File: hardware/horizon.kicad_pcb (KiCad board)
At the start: 2 copper layers, 95 x 56.2 mm, 31 parts, among them J1 Conn_01x02_Pin, J2 Conn_01x06_Pin, J3 USB_C_Receptacle_USB2.0_14P, J4 Conn_01x14_Pin, J6 Conn_01x02_Pin, SW1 SW_Push, U1 ESP32-S3, U2 NCP1529A, U3 W25Q128JVS, U4 BQ24074RGT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

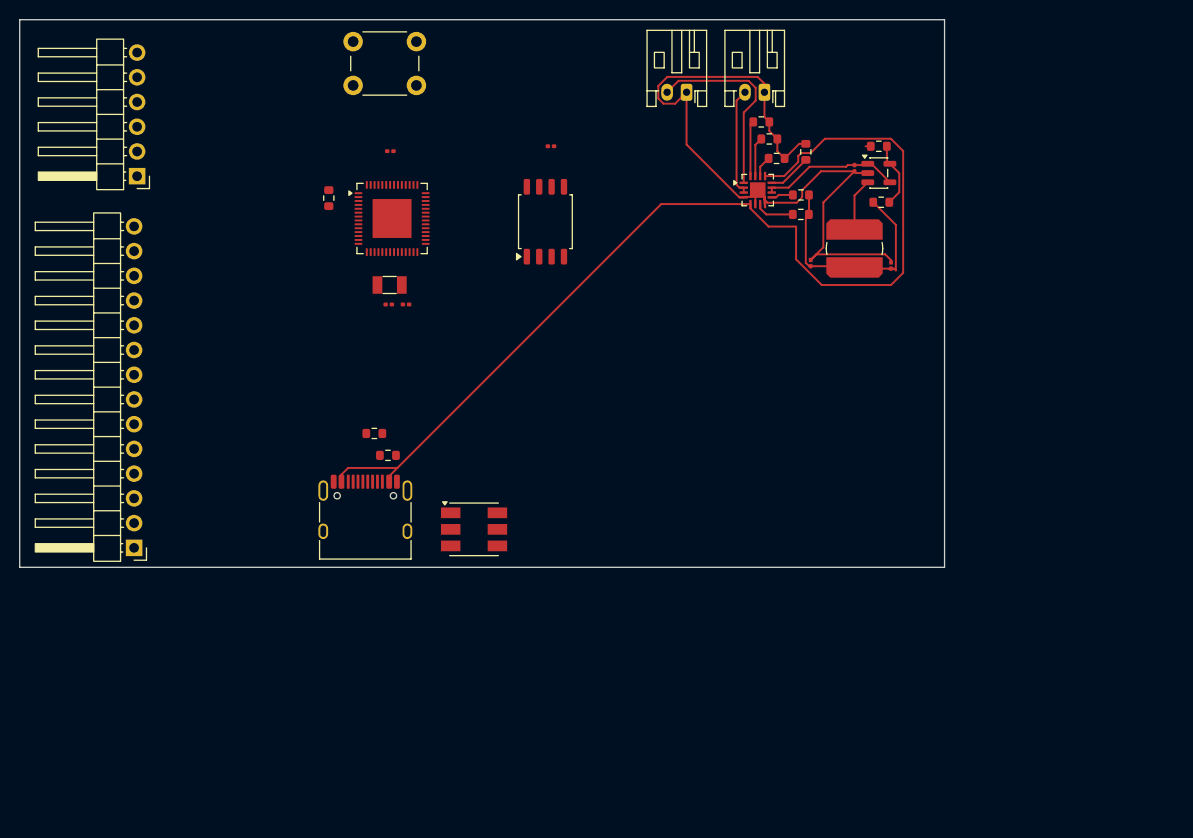
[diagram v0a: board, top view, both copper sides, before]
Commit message: added antenna
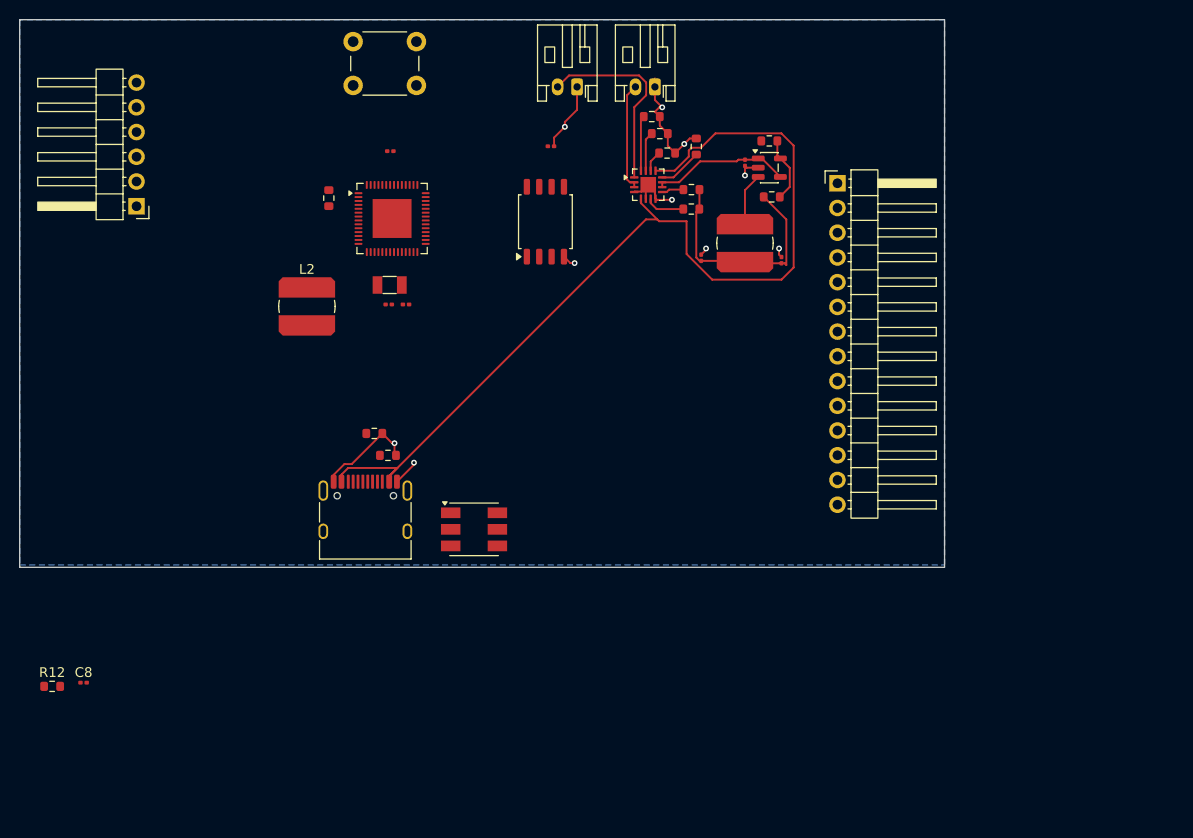
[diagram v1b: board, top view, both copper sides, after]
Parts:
- added C8: DNP, Capacitor_SMD:C_0201_0603Metric, F.Cu at (96.6, 93.1)
- added L2: DNP, Inductor_SMD:L_Bourns_SDR0604, F.Cu at (119.5, 54.5)
- added R12: 0R, Resistor_SMD:R_0603_1608Metric, F.Cu at (93.3, 93.5)
- moved J4 81.4 mm to (174.0, 41.8), turned to 0 degrees
- moved C3 11.3 mm to (164.5, 39.7)
- moved C4 11.3 mm to (168.2, 49.7)
- moved C5 11.3 mm to (160.0, 49.5)
- moved J1 11.3 mm to (147.2, 31.9)
- moved J6 11.3 mm to (155.2, 31.9)
- moved L1 11.3 mm to (164.5, 48.0)
- moved R1 11.3 mm to (167.2, 43.2)
- moved R10 11.3 mm to (159.0, 44.5)
- moved R11 11.3 mm to (156.5, 38.7)
- moved R2 11.3 mm to (167.0, 37.5)
- moved R6 11.3 mm to (159.5, 38.0)
- moved R7 11.3 mm to (154.9, 35.0)
- moved R8 11.3 mm to (155.8, 36.7)
- moved R9 11.3 mm to (159.0, 42.5)
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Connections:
- U1 pad 1: unconnected-(U1-LNA_IN-Pad1) -> Net-(U1-LNA_IN)
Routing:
- net GND: track 81.4 -> 46.7 mm, vias 0 -> 10
- net Net-(U4-EN2): track 107.1 -> 98.0 mm
- added copper zone on B.Cu, net GND

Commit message: Finished prototype pcb
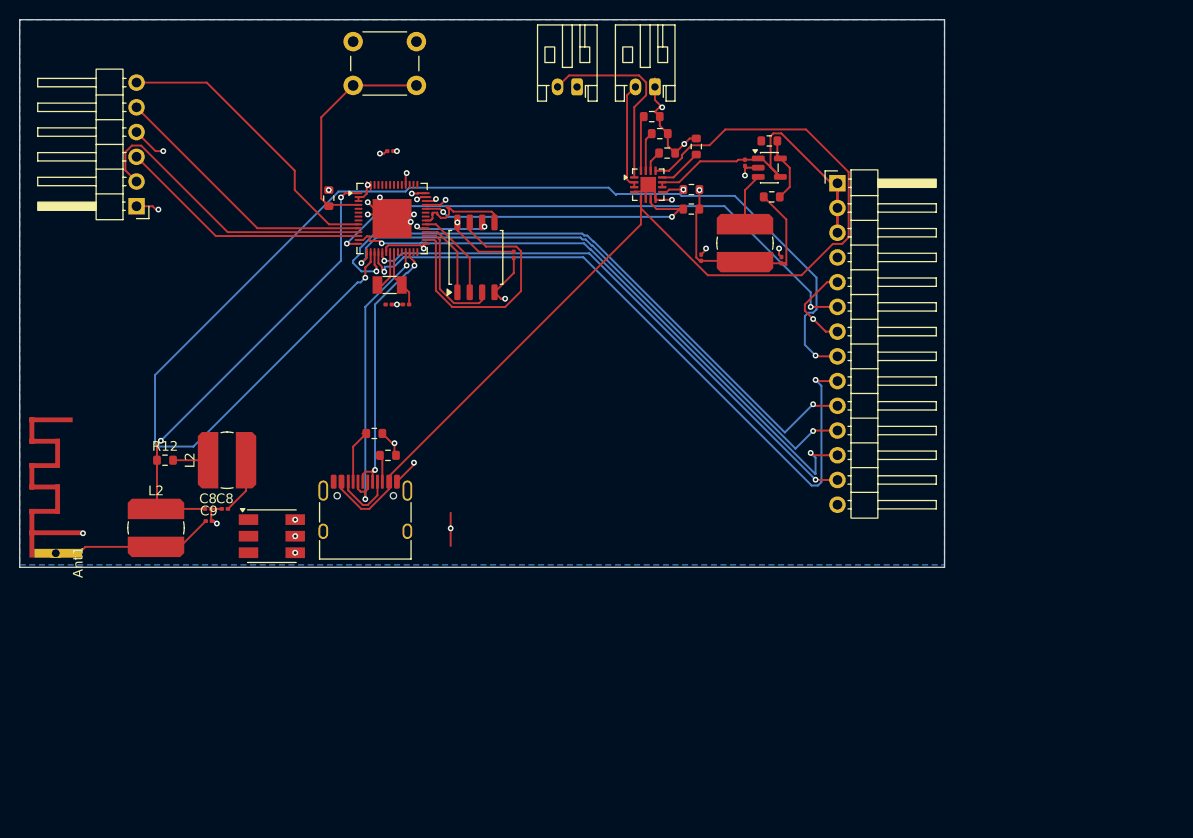
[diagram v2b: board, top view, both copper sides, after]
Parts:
- added Ant1: PCB_Antenna:PCB_Antenna, PCB_Antenna:PCB_Antenna, F.Cu at (96.5, 80.8)
- added C8: 3P3, Capacitor_SMD:C_0201_0603Metric, F.Cu at (109.3, 75.2)
- added C9: 3P3, Capacitor_SMD:C_0201_0603Metric, F.Cu at (109.4, 76.5)
- added L2: 2n2, Inductor_SMD:L_Bourns_SDR0604, F.Cu at (104.0, 77.2)
- moved R12 26.0 mm to (104.9, 70.2)
- moved C8 23.0 mm to (111.1, 75.2)
- moved Status1 20.8 mm to (115.9, 78.0)
- moved L2 17.8 mm to (111.3, 70.2), turned to 90 degrees
- moved C2 11.8 mm to (140.8, 49.2), turned to -90 degrees
- moved U3 8.02 mm to (136.9, 49.4)
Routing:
- net SPI_MOSI: track 0.00 -> 130.1 mm, vias 0 -> 2
- net SPI_MISO: track 0.00 -> 71.0 mm, vias 0 -> 2
- net SPI_CLK: track 0.00 -> 66.0 mm, vias 0 -> 2
- net SPI_RESET: track 0.00 -> 62.8 mm, vias 0 -> 2
- net SPI_CS0: track 0.00 -> 61.7 mm, vias 0 -> 2
- net SPI_POWERCTRL: track 0.00 -> 58.4 mm, vias 0 -> 2
- net SPI_HOSTHRDY: track 0.00 -> 57.5 mm, vias 0 -> 2
- net Net-(U1-LNA_IN): track 0.00 -> 46.9 mm, vias 0 -> 2
- net Net-(Status1-BA): track 0.00 -> 44.8 mm, vias 0 -> 2
- net Net-(Status1-GA): track 0.00 -> 42.2 mm, vias 0 -> 2
- net Net-(Status1-RA): track 0.00 -> 40.1 mm, vias 0 -> 2
- net Touch-INT: track 0.00 -> 31.4 mm
- net USB_D-: track 0.00 -> 30.7 mm, vias 0 -> 2
- net Touch-SDA: track 0.00 -> 30.0 mm
- net Touch-SCL: track 0.00 -> 27.9 mm
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- added copper zone on In2.Cu, net +3.3V
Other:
- copper layers 2 -> 4

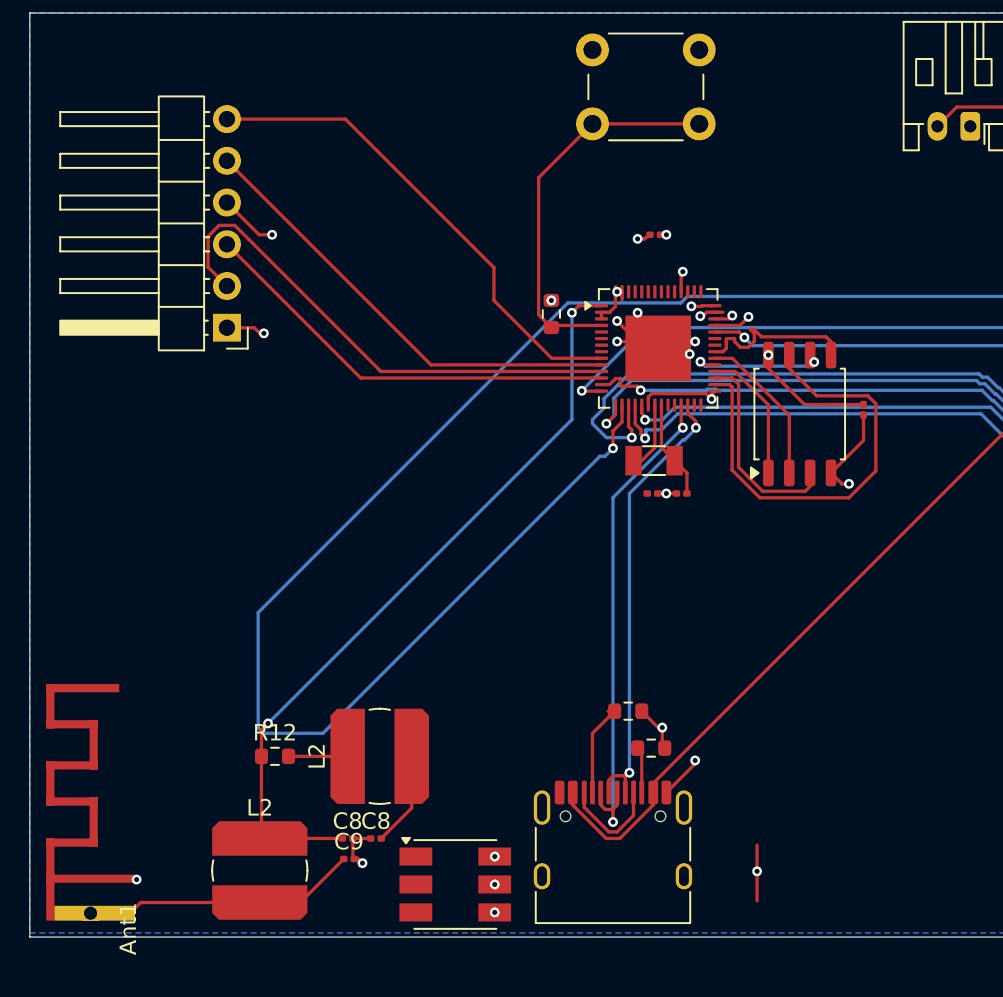
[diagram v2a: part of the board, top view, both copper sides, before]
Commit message: Added haptic and sleep button
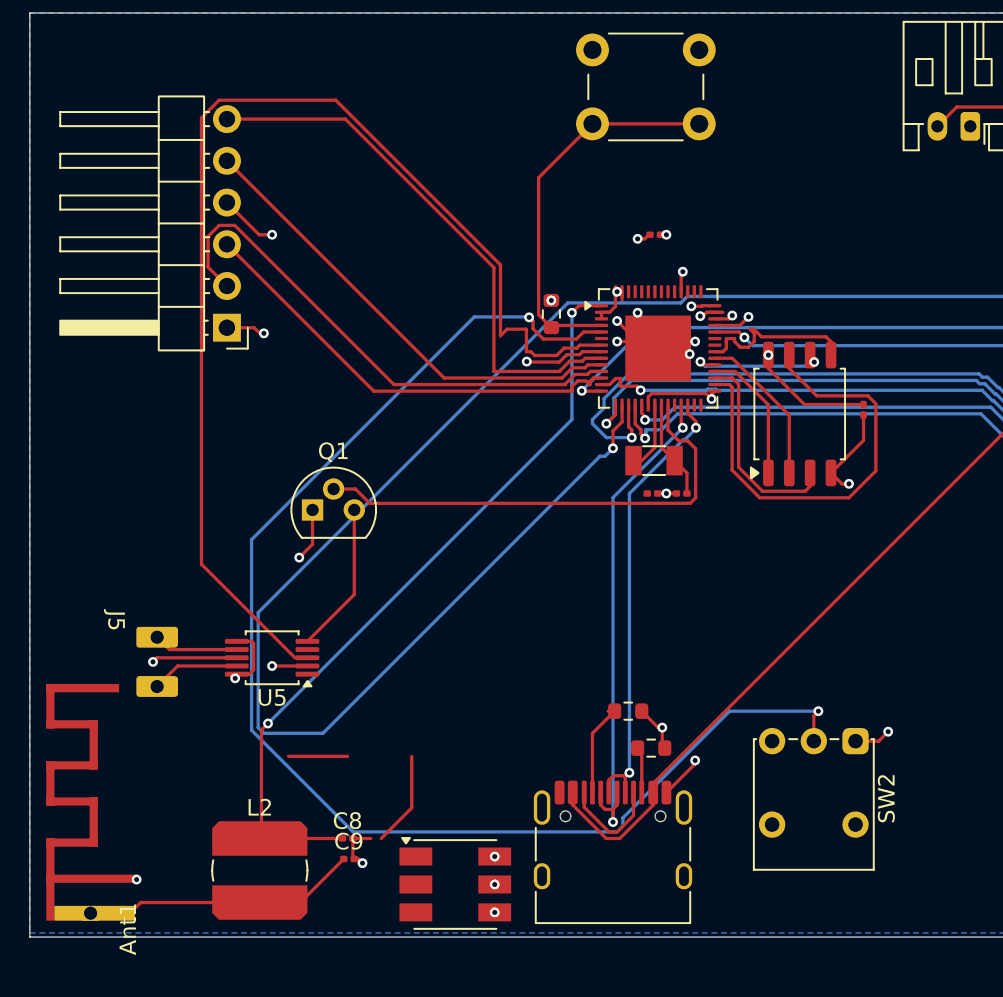
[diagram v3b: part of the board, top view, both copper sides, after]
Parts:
- removed the C8 at (111.1, 75.2)
- removed the L2 at (111.3, 70.2)
- removed R12: 0R, Resistor_SMD:R_0603_1608Metric
- added J5: Conn_01x02_Socket, Solder Pads:2x solder pads, F.Cu at (94.8, 62.0)
- added Q1: NPN, Package_TO_SOT_THT:TO-92L, F.Cu at (107.2, 55.2)
- added SW2: SW_Push, Button_Switch_THT:SW_Push_1P2T_Vertical_E-Switch_800UDP8P1A1M6, F.Cu at (140.3, 69.3)
- added U5: DRV2605LDGS, Package_SO:TSSOP-10_3x3mm_P0.5mm, F.Cu at (104.8, 64.2)
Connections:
- U1 pad 23: unconnected-(U1-GPIO17-Pad23) -> HAPTIC_SLEEP
- U1 pad 5: unconnected-(U1-GPIO0-Pad5) -> Net-(U1-GPIO0)
- U1 pad 7: unconnected-(U1-GPIO2-Pad7) -> HAPTIC_SDA
- U1 pad 8: unconnected-(U1-GPIO3-Pad8) -> HAPTIC_SCL
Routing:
- net Net-(U1-GPIO0): track 0.00 -> 81.9 mm, vias 0 -> 2
- net HAPTIC_SDA: track 0.00 -> 71.1 mm
- net HAPTIC_SCL: track 0.00 -> 32.4 mm, vias 0 -> 2
- net HAPTIC_SLEEP: track 0.00 -> 29.2 mm
- net (no net): track 6.32 -> 15.7 mm, vias 0 -> 3
- net Net-(Q1-E): track 0.00 -> 9.18 mm
- net +3.3V: track 46.4 -> 52.7 mm, vias 8 -> 10
- net Net-(AE1-A): track 5.77 -> 0.00 mm
- net Net-(J5-Pin_2): track 0.00 -> 5.37 mm
- net Net-(J5-Pin_1): track 0.00 -> 5.16 mm
- net GND: track 69.1 -> 74.1 mm, vias 23 -> 24
- net Net-(L2-Pad1): track 3.60 -> 0.00 mm
- net Touch-SDA: track 30.0 -> 33.2 mm
- net Touch-RST: track 26.2 -> 27.3 mm
- net Touch-INT: track 31.4 -> 32.1 mm
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
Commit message: Redoing pcb and fixed schem
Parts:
- added C10: 0.1uF, Capacitor_SMD:C_0201_0603Metric, F.Cu at (119.9, 52.1)
- added C11: 1uF, Capacitor_SMD:C_0201_0603Metric, F.Cu at (117.0, 55.9)
- added C12: 1uF, Capacitor_SMD:C_0201_0603Metric, F.Cu at (116.8, 54.5)
- added C13: 1uF, Capacitor_SMD:C_0201_0603Metric, F.Cu at (122.0, 64.9)
- added C14: 10nF, Capacitor_SMD:C_0201_0603Metric, F.Cu at (117.8, 90.9)
- added C15: 0.1uF, Capacitor_SMD:C_0201_0603Metric, F.Cu at (125.9, 64.8)
- added C16: 1uF, Capacitor_SMD:C_0201_0603Metric, F.Cu at (130.2, 72.7)
- added C17: 0.1uF, Capacitor_SMD:C_0201_0603Metric, F.Cu at (128.9, 72.6)
- added C18: 0.1uF, Capacitor_SMD:C_0201_0603Metric, F.Cu at (123.4, 75.9)
- added C19: TBD, Capacitor_SMD:C_0201_0603Metric, F.Cu at (103.2, 72.1)
- added D2: D_TVS, Diode_SMD:D_0402_1005Metric, F.Cu at (104.3, 78.7)
- added D3: D_TVS, Diode_SMD:D_0402_1005Metric, F.Cu at (113.5, 76.3)
- added L3: L, Inductor_SMD:L_Bourns_SDR0604, F.Cu at (121.2, 56.6)
- added L4: TBD, Inductor_SMD:L_Bourns_SDR0604, F.Cu at (107.1, 72.7)
- added REF**: MountingHole_2.2mm_M2, MountingHole:MountingHole_2.2mm_M2, F.Cu at (114.8, 99.9)
- added REF**: MountingHole_2.2mm_M2, MountingHole:MountingHole_2.2mm_M2, F.Cu at (183.9, 90.9)
- added REF**: MountingHole_2.2mm_M2, MountingHole:MountingHole_2.2mm_M2, F.Cu at (116.2, 63.2)
- added REF**: MountingHole_2.2mm_M2, MountingHole:MountingHole_2.2mm_M2, F.Cu at (184.2, 63.5)
- added U6: ESP-PSRAM64H, Package_SO:SOIC-8_5.3x5.3mm_P1.27mm, F.Cu at (131.4, 60.0)
- C1: value 100nF -> 0.1uF; footprint Capacitor_SMD:C_0201_0603Metric -> Diode_SMD:D_0402_1005Metric
- C2: value 100nF -> 10uF
- C8, C9: value 3P3 -> TBD
- L2: value 2n2 -> TBD
- moved J5 64.2 mm to (157.3, 76.4), turned to 90 degrees
- moved J4 57.6 mm to (193.7, 95.9), turned to -90 degrees
- moved Q1 54.7 mm to (155.6, 80.7), turned to 180 degrees
- moved L1 54.2 mm to (128.6, 88.5)
- moved J2 51.6 mm to (113.9, 94.3)
- moved C3 51.3 mm to (138.2, 83.7), turned to 0 degrees
- moved R2 51.0 mm to (140.3, 81.0), turned to -90 degrees
- moved U2 50.9 mm to (136.3, 80.7)
- moved J1 50.6 mm to (190.5, 58.3)
- moved C2 46.4 mm to (104.0, 77.5), turned to 0 degrees
- moved R1 45.2 mm to (142.5, 81.0), turned to 90 degrees
- moved U5 42.5 mm to (145.4, 76.4), turned to 0 degrees
- moved C1 39.6 mm to (117.4, 76.6), turned to 180 degrees
- moved C4 39.1 mm to (139.7, 76.4), turned to 0 degrees
- moved J6 38.0 mm to (182.5, 58.3)
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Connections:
- Ant1 pad 1: Net-(Ant1-Pad1) -> Net-(D3-A1)
- C1 pad 1: +3.3V -> Net-(C1-Pad1)
- C2 pad 1: +3.3V -> VDD_SPI
- C4 pad 1: +3.3V -> VDD_SPI
- C5 pad 1: +3.3V -> VDD_SPI
- C9 pad 1: Net-(Ant1-Pad1) -> Net-(C19-Pad1)
- J2 pad 4: +3.3V -> VDD_SPI
- L1 pad 2: +3.3V -> VDD_SPI
- L2 pad 2: Net-(Ant1-Pad1) -> Net-(C19-Pad1)
- R1 pad 2: +3.3V -> VDD_SPI
- R10 pad 2: +3.3V -> VDD_SPI
- R3 pad 2: +3.3V -> VDD_SPI
- R9 pad 2: +3.3V -> VDD_SPI
- SW2 pad 1: +3.3V -> VDD_SPI
- U1 pad 2: +3.3V -> Net-(C1-Pad1)
- U1 pad 20: +3.3V -> VDD_SPI
- U1 pad 29: +3.3V -> VDD_SPI
- U1 pad 3: +3.3V -> Net-(C1-Pad1)
- U1 pad 46: +3.3V -> VDD_SPI
- U1 pad 55: +3.3V -> VDD_SPI
- U1 pad 56: +3.3V -> VDD_SPI
- U3 pad 8: +3.3V -> VDD_SPI
- U5 pad 10: +3.3V -> VDD_SPI
- U5 pad 6: +3.3V -> VDD_SPI
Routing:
- net VDD_SPI: track 0.00 -> 244.5 mm, vias 0 -> 9
- net +5V: track 37.9 -> 108.8 mm, vias 0 -> 3
- net CHG: track 30.0 -> 96.1 mm
- net SPI_MOSI: track 130.1 -> 76.9 mm
- net +3.3V: track 52.7 -> 0.00 mm, vias 10 -> 0
- net Net-(U1-LNA_IN): track 46.9 -> 0.00 mm, vias 2 -> 0
- net HAPTIC_SDA: track 71.1 -> 28.0 mm, vias 0 -> 3
- net USB_D-: track 30.7 -> 68.4 mm
- net QSPI_CLK: track 8.63 -> 45.6 mm, vias 2 -> 0
- net Net-(U1-GPIO0): track 81.9 -> 49.3 mm, vias 2 -> 4
- net Net-(C1-Pad1): track 0.00 -> 31.1 mm
- net GND: track 74.1 -> 101.0 mm, vias 24 -> 30
- net Net-(D3-A1): track 0.00 -> 26.8 mm
- net PGOOD: track 31.2 -> 57.7 mm
- net USB_D+: track 27.6 -> 52.5 mm
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- added copper zone on In1.Cu, net GND
- removed copper zone on In2.Cu, net +3.3V
- removed copper zone on B.Cu, net GND

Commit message: Finished pcb!
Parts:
- moved C1 4.09 mm to (113.5, 75.2)
- moved REF** 2.22 mm to (114.8, 61.5)
- moved C10 0.85 mm to (119.9, 53.0)
- moved C15 0.12 mm to (126.0, 64.8)
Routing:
- net Net-(C1-Pad1): track 31.1 -> 48.9 mm, vias 0 -> 2
- net Net-(U1-LNA_IN): track 0.00 -> 17.6 mm
- net Net-(U4-EN2): track 81.1 -> 89.1 mm
- net VDD_SPI: track 244.5 -> 251.5 mm
- net GND: track 101.0 -> 105.1 mm
- net Net-(J3-CC2): track 0.00 -> 3.31 mm
